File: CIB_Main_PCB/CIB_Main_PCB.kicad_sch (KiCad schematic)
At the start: 24 parts, among them J10 ISO MON, J15 DUT PSU, J16 CIB Interface

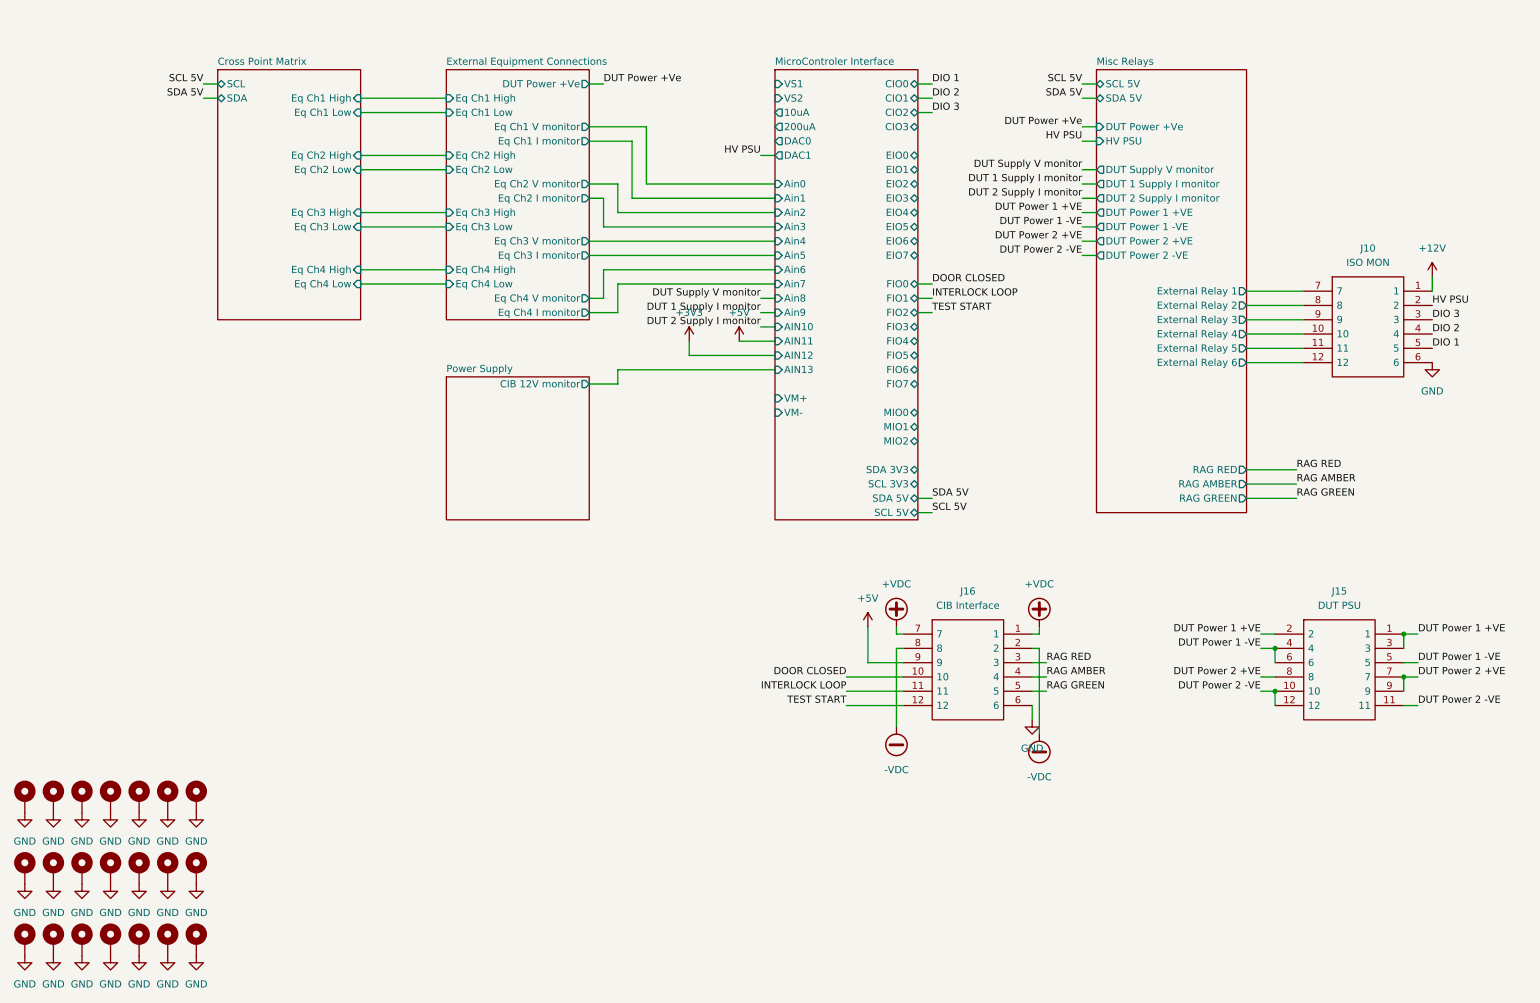
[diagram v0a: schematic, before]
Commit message: added snubbing to the relays
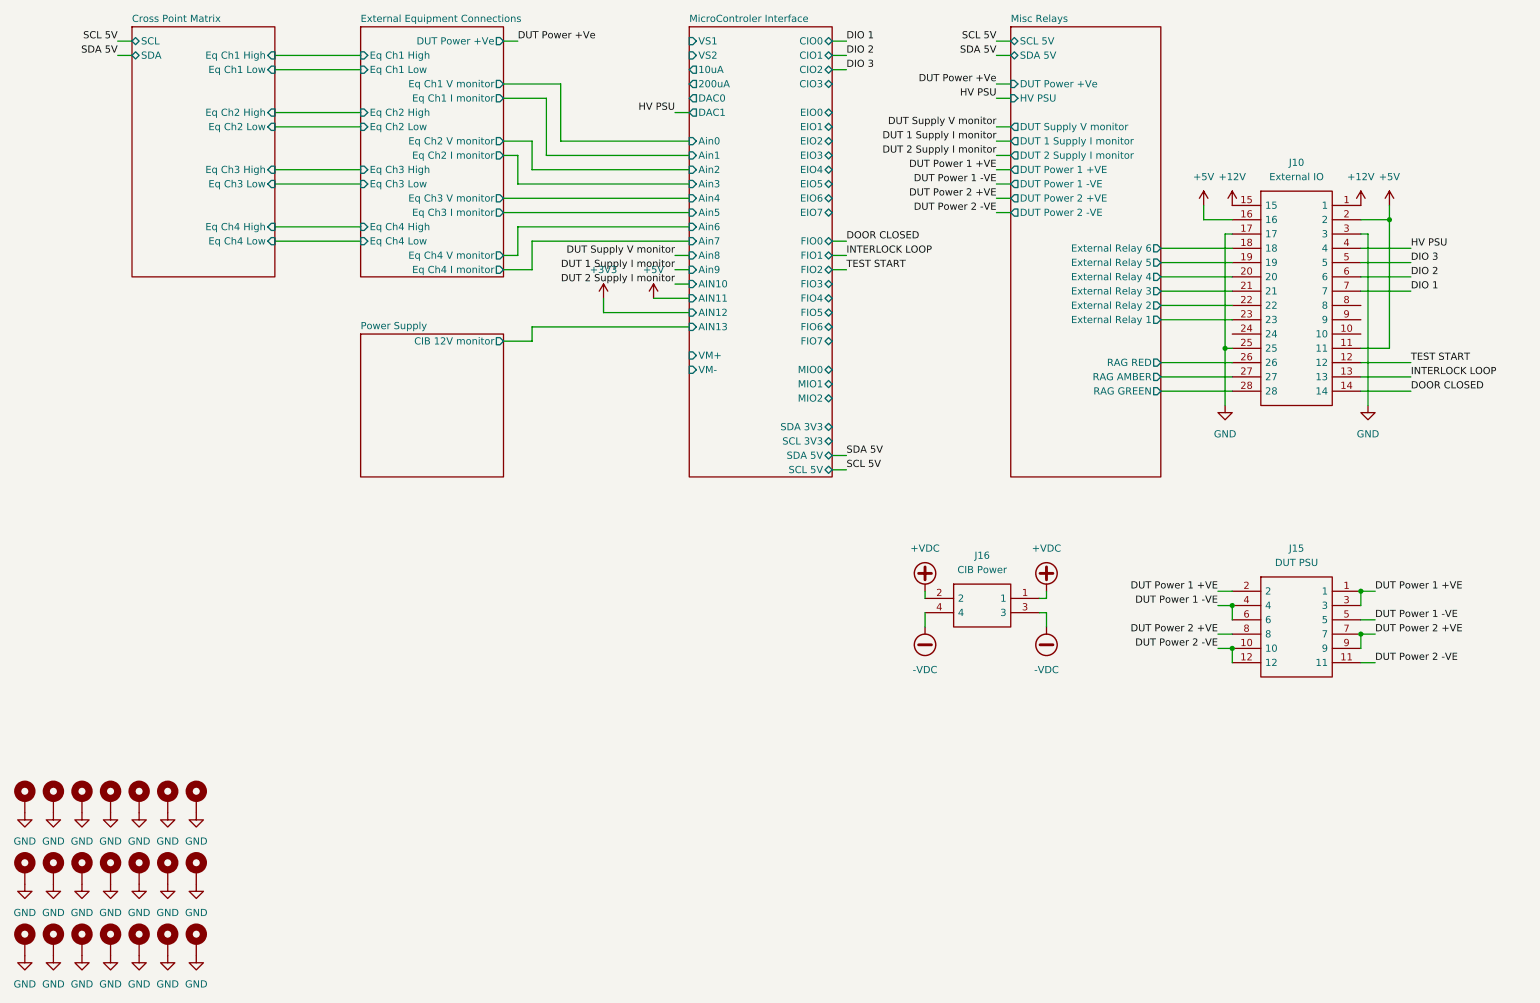
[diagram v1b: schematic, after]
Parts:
- J10: value ISO MON -> External IO; footprint Component Search Engine:Pluggable Terminal Blocks SDDC 1,5 6-PV-3,5 -> Component Search Engine:Pluggable Terminal Blocks SDDC 1,5 14-PV-3,5; symbol Component Search Engine:Pluggable Terminal Blocks SDDC 1,5/ 6-PV-3,5 -> Component Search Engine:Pluggable Terminal Blocks SDDC 1,5/ 14-PV-3,5; Manufacturer_Part_Number (none) -> 1848765; Mouser Part Number 651-1848684 -> 651-1848765; Mouser Price/Stock https://www.mouser.co.uk/ProductDetail/Phoenix-Contact/1848684?qs=0kYgdqhPduG4EaaFk8CcwA%3D%3D -> https://www.mouser.co.uk/ProductDetail/Phoenix-Contact/1848765?qs=0kYgdqhPduEzMECWyGhNIA%3D%3D
- J16: value CIB Interface -> CIB Power; footprint Component Search Engine:Pluggable Terminal Blocks SDDC 1,5 6-PV-3,5 -> 1864053; symbol Component Search Engine:Pluggable Terminal Blocks SDDC 1,5/ 6-PV-3,5 -> Component Search Engine:Pluggable Terminal Blocks SDC 2,5/ 4-PV-5,0 0-ZB; Arrow Part Number 1848684 -> 1864053; Arrow Price/Stock https://www.arrow.com/en/products/1848684/phoenix-contact?r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 -> https://www.arrow.com/en/products/1864053/phoenix-contact; Manufacturer_Part_Number (none) -> 1864053; Mouser Part Number 651-1848684 -> 651-1864053; Mouser Price/Stock https://www.mouser.co.uk/ProductDetail/Phoenix-Contact/1848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 -> https://www.mouser.co.uk/ProductDetail/Phoenix-Contact/1864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
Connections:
- net RAG AMBER is gone; now on net -VDC: J16.4
- net RAG RED is gone; now on net -VDC: J16.3
- net +12V: now also J10.15
- net +5V: now also J10.11, J10.16, J10.2; no longer J16.9
- net +VDC: now also J16.2; no longer J16.7
- net -VDC: no longer J16.2, J16.8
- net DIO 1: now also J10.7; no longer J10.5
- net DIO 2: now also J10.6; no longer J10.4
- net DIO 3: now also J10.5; no longer J10.3
- net DOOR CLOSED: now also J10.14; no longer J16.10
- net GND: now also J10.17, J10.25, J10.3; no longer J10.6, J16.6
- net HV PSU: now also J10.4; no longer J10.2
- net INTERLOCK LOOP: now also J10.13; no longer J16.11
- net Misc Relays/External Relay 1: now also J10.23; no longer J10.7
- net Misc Relays/External Relay 2: now also J10.22; no longer J10.8
- net Misc Relays/External Relay 3: now also J10.21; no longer J10.9
- net Misc Relays/External Relay 4: now also J10.20; no longer J10.10
- net Misc Relays/External Relay 5: now also J10.19; no longer J10.11
- net Misc Relays/External Relay 6: now also J10.18; no longer J10.12
- net TEST START: now also J10.12; no longer J16.12
- removed net RAG GREEN: J16.5
- new net Misc Relays/RAG AMBER: J10.27
- new net Misc Relays/RAG GREEN: J10.28
- new net Misc Relays/RAG RED: J10.26
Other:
- moved on the sheet: J15
